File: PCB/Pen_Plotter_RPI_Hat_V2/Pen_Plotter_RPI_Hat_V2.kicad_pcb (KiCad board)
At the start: 4 copper layers, 85 x 56 mm, 28 parts, among them J1 RASM712PX, J2 X_LIMIT_SWITCH, J3 X-AXIS_STEPPER, J4 Y_LIMIT_SWITCH, J5 SERVO, J6 Y-AXIS_STEPPER, J7 PAPER_SENSOR, J8 DC_MOTOR, U2 MINI560, U4 X-AXIS_DRV8825_STEPPER_MOTOR_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, U5 Y-AXIS_DRV8825_STEPPER_MOTOR_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, U6 RPI3-MODBP-BULK, U7 LM393AN, U9 ATmega328P-P

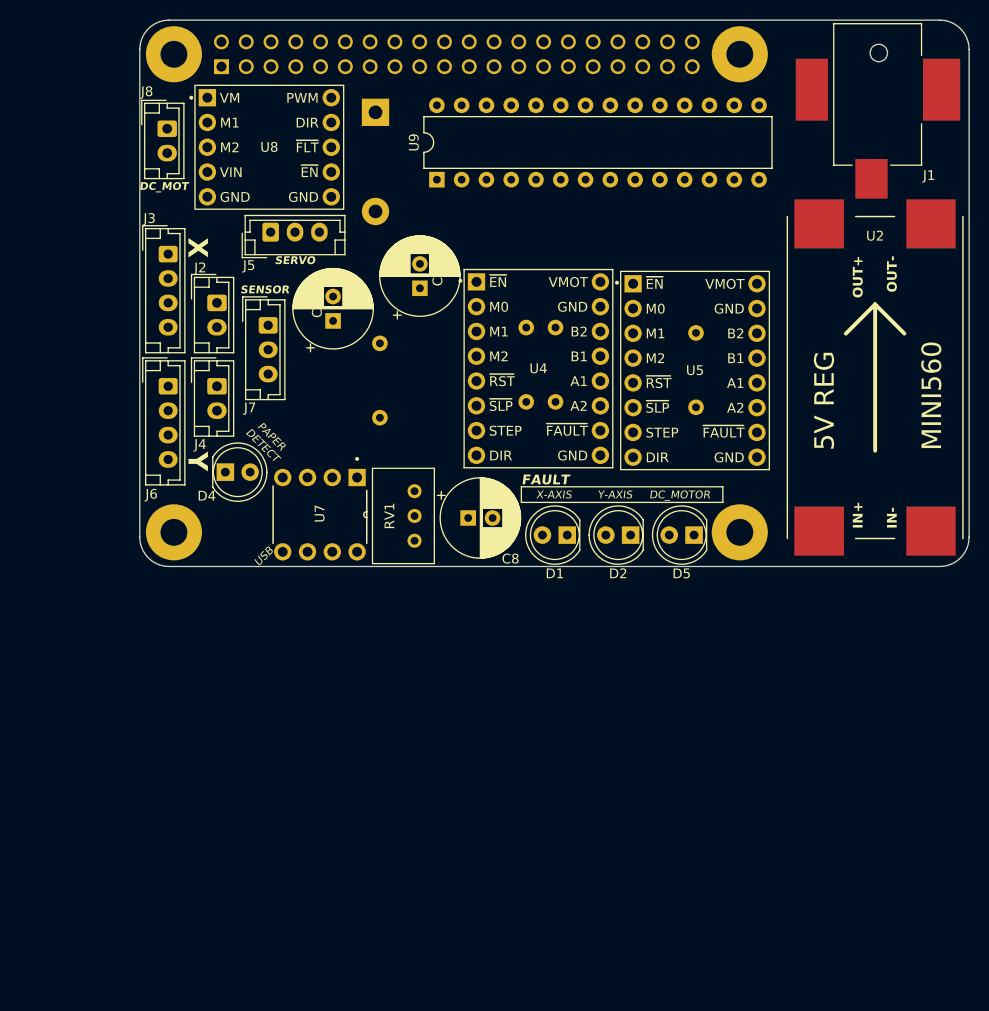
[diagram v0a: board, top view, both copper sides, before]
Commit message: Added third stepper motor driver
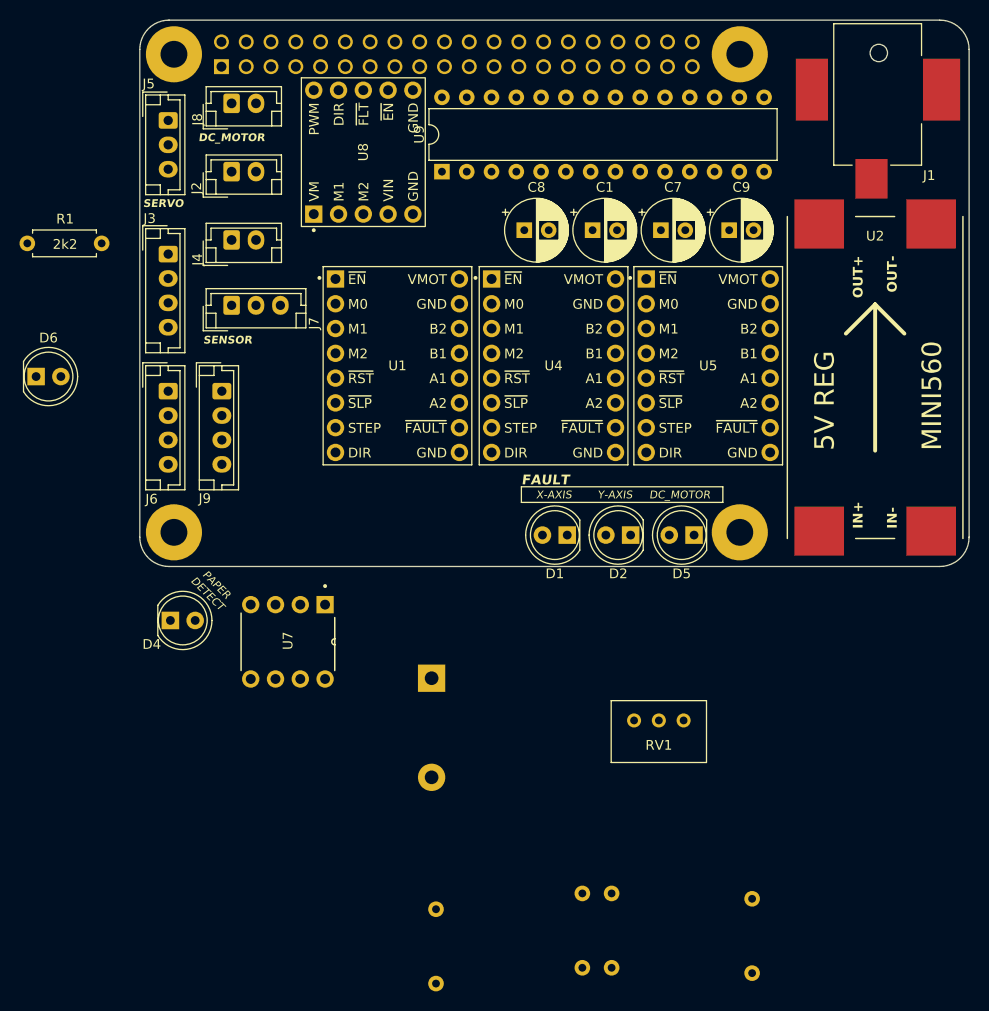
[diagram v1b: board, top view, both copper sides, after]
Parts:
- added C1: 100u, Capacitor_THT:CP_Radial_D6.3mm_P2.50mm, F.Cu at (102.5, 56.0)
- added D6: RED, LED_THT:LED_D5.0mm, F.Cu at (45.5, 71.0)
- added J9: EXTRA_STEPPER, Connector_JST:JST_EH_B4B-EH-A_1x04_P2.50mm_Vertical, F.Cu at (64.5, 72.5)
- added R1: 2k2, Pen_Plotter_Lib:THT_RESISTOR_WITH_VALUE, F.Cu at (48.4, 57.5)
- added U1: EXTRA_DRV8825_STEPPER_MOTOR_DRIVER_CARRIER, Pen_Plotter_Lib:IC_DRV8825_STEPPER_MOTOR_DRIVER_CARRIER, F.Cu at (82.5, 69.9)
- C7, C8, C9: footprint Capacitor_THT:CP_Radial_D8.0mm_P2.50mm -> Capacitor_THT:CP_Radial_D6.3mm_P2.50mm
- moved D3 58.3 mm to (86.0, 101.9)
- moved R3 58.3 mm to (101.5, 127.8)
- moved R4 58.3 mm to (104.5, 127.8)
- moved R5 58.3 mm to (86.5, 129.5)
- moved R6 58.3 mm to (119.0, 128.4)
- moved C7 34.9 mm to (109.5, 56.0), turned to 0 degrees
- moved RV1 33.2 mm to (111.8, 106.2), turned to 0 degrees
- moved C9 32.3 mm to (116.5, 56.0), turned to 0 degrees
- moved C8 30.1 mm to (95.5, 56.0)
- moved D4 16.2 mm to (59.2, 96.0)
- moved J5 15.5 mm to (59.0, 44.8), turned to -90 degrees
- moved J4 15.1 mm to (65.5, 57.0), turned to 0 degrees
- moved J2 13.5 mm to (65.5, 50.0), turned to 0 degrees
- moved U7 13.4 mm to (67.5, 102.0)
- moved U8 9.65 mm to (79.0, 48.0), turned to 90 degrees
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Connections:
- J3 pad 1: /Stepper Motors/X-AXIS_A1 -> /Stepper Motors/X-AXIS_A2
- J3 pad 2: /Stepper Motors/X-AXIS_A2 -> /Stepper Motors/X-AXIS_A1
- J6 pad 1: /Stepper Motors/Y-AXIS_A1 -> /Stepper Motors/Y-AXIS_A2
- J6 pad 2: /Stepper Motors/Y-AXIS_A2 -> /Stepper Motors/Y-AXIS_A1
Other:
- board text removed: "DC_MOT"
- board text removed: "USB"
- board text removed: "X"
- board text removed: "Y"

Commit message: Completed PCB layout
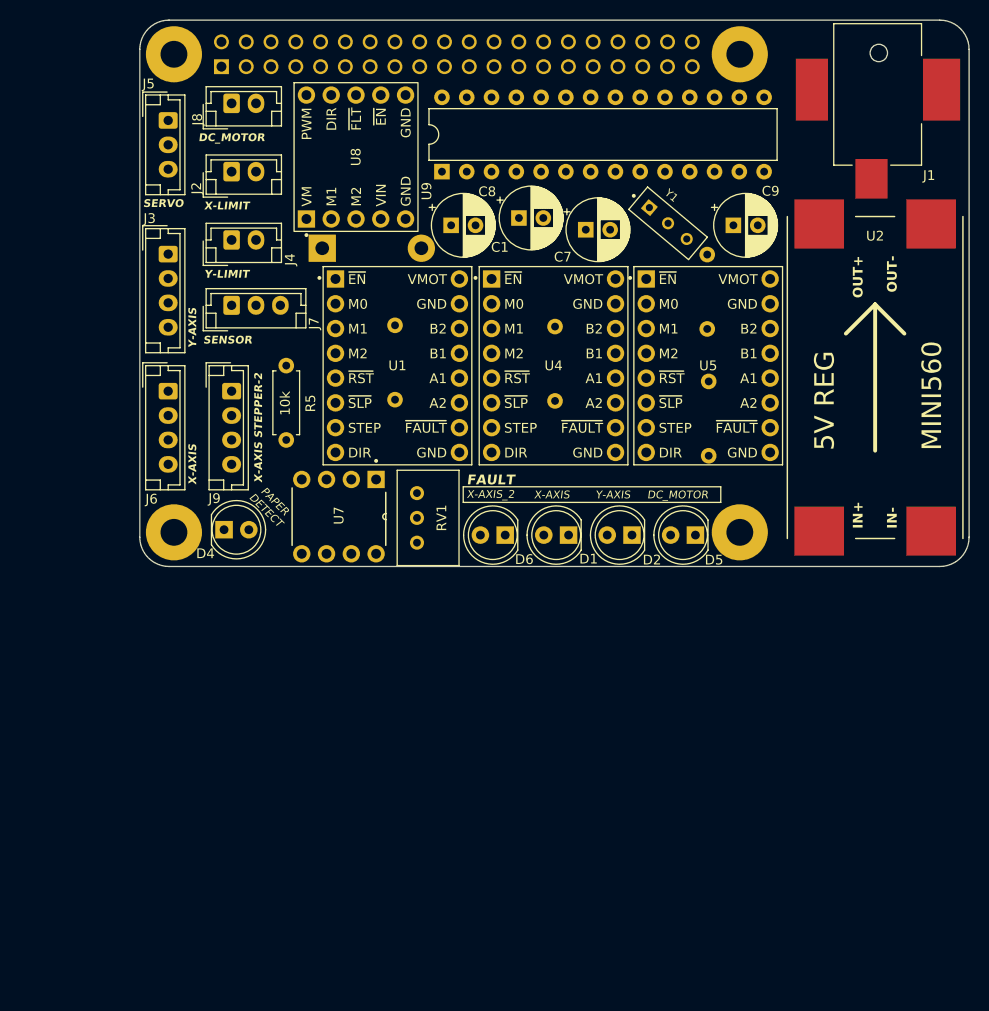
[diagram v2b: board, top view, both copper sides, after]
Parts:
- added Y1: CSTLS8M00G56-A0, Pen_Plotter_Lib:OSC_CSTLS8M00G56-A0, F.Cu at (110.2, 55.3)
- R1: moved to B.Cu
- R5: moved to F.Cu
- moved R6 66.2 mm to (114.3, 62.4)
- moved R3 58.2 mm to (98.8, 69.8)
- moved R5 57.8 mm to (71.0, 73.8)
- moved R4 53.4 mm to (114.5, 75.4)
- moved D6 50.8 mm to (93.5, 87.2), turned to 180 degrees
- moved D3 45.5 mm to (74.8, 57.9), turned to 0 degrees
- moved RV1 35.9 mm to (84.5, 83.0), turned to 90 degrees
- moved R1 35.8 mm to (82.2, 69.5), turned to 90 degrees
- moved U7 13.9 mm to (72.7, 89.2)
- moved D4 10.8 mm to (64.7, 86.7)
- moved C7 7.70 mm to (101.8, 56.0)
- moved C1 7.65 mm to (95.0, 54.8)
- moved C8 7.52 mm to (88.0, 55.5)
- moved J9 1.00 mm to (65.5, 72.5)
- moved U8 0.90 mm to (78.2, 48.5)
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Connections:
- U9 pad 10: unconnected-(U9-XTAL2/PB7-Pad10) -> Net-(U9-XTAL2/PB7)
- U9 pad 9: unconnected-(U9-XTAL1/PB6-Pad9) -> Net-(U9-XTAL1/PB6)
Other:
- board text added: "X-AXIS STEPPER-2"
- board text added: "X-AXIS_2"
- board text added: "X-LIMIT"
- board text added: "Y-LIMIT"

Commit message: Manually added traces for high current
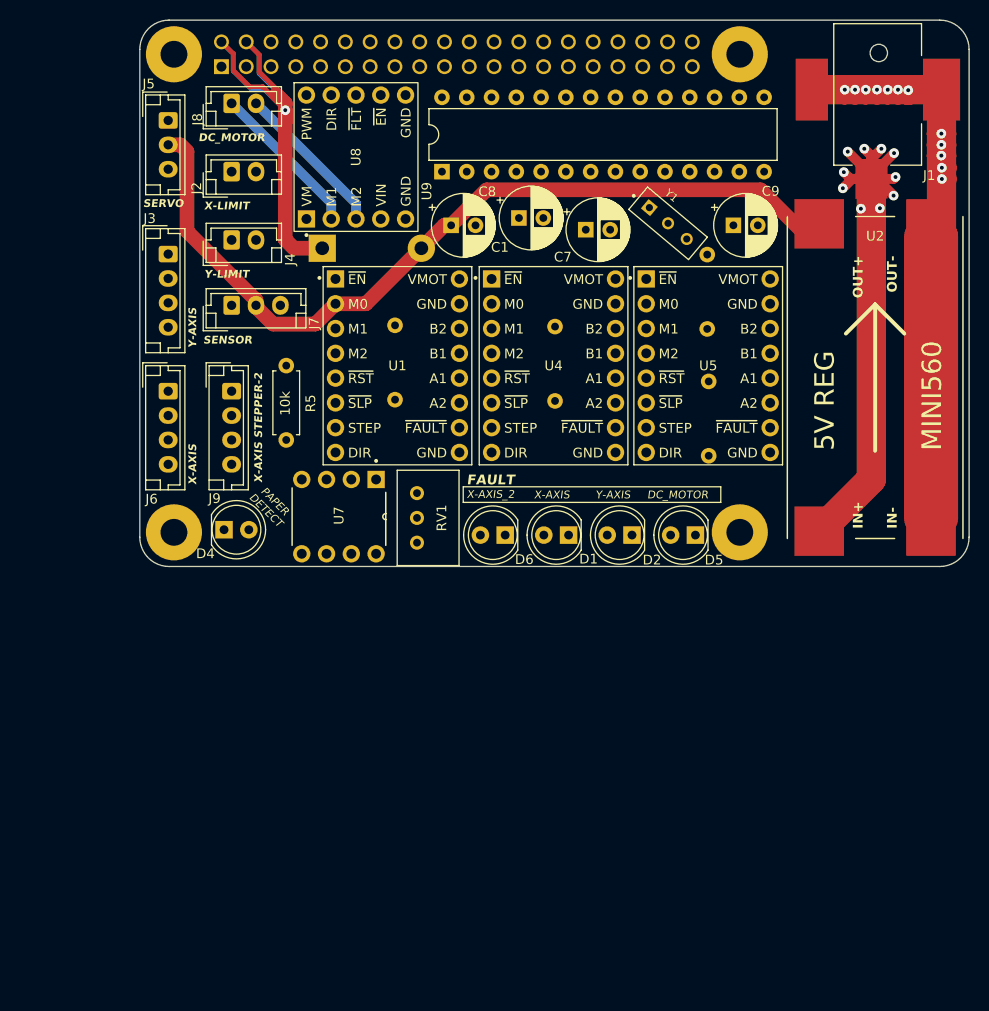
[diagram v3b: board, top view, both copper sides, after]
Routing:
- net GND: track 0.00 -> 86.5 mm, vias 0 -> 12
- net +5V: track 0.00 -> 85.9 mm
- net +12V: track 0.00 -> 69.7 mm, vias 0 -> 10
- net Net-(D3-K): track 0.00 -> 55.7 mm, vias 0 -> 1
- net Net-(J8-Pin_2): track 0.00 -> 16.1 mm
- net Net-(J8-Pin_1): track 0.00 -> 16.1 mm

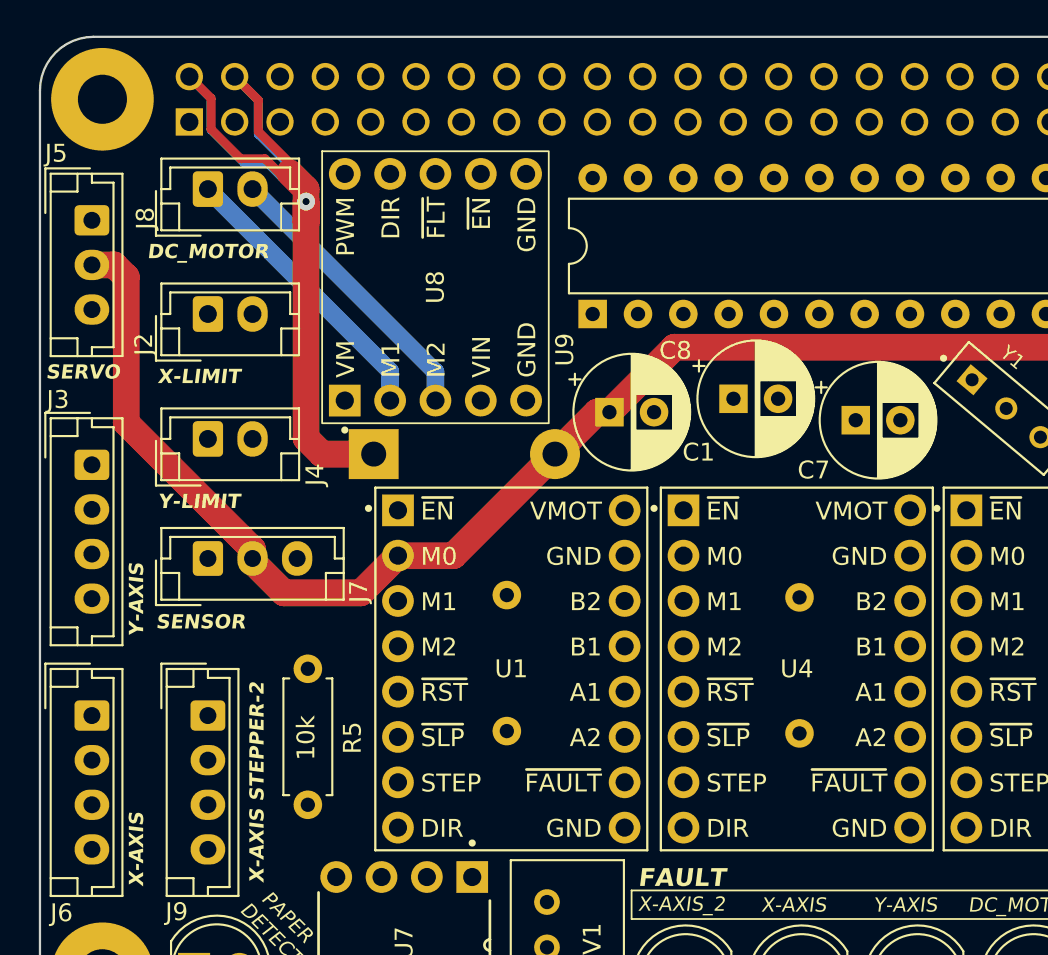
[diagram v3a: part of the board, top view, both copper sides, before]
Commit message: Changed layout and footprints to make routing easier
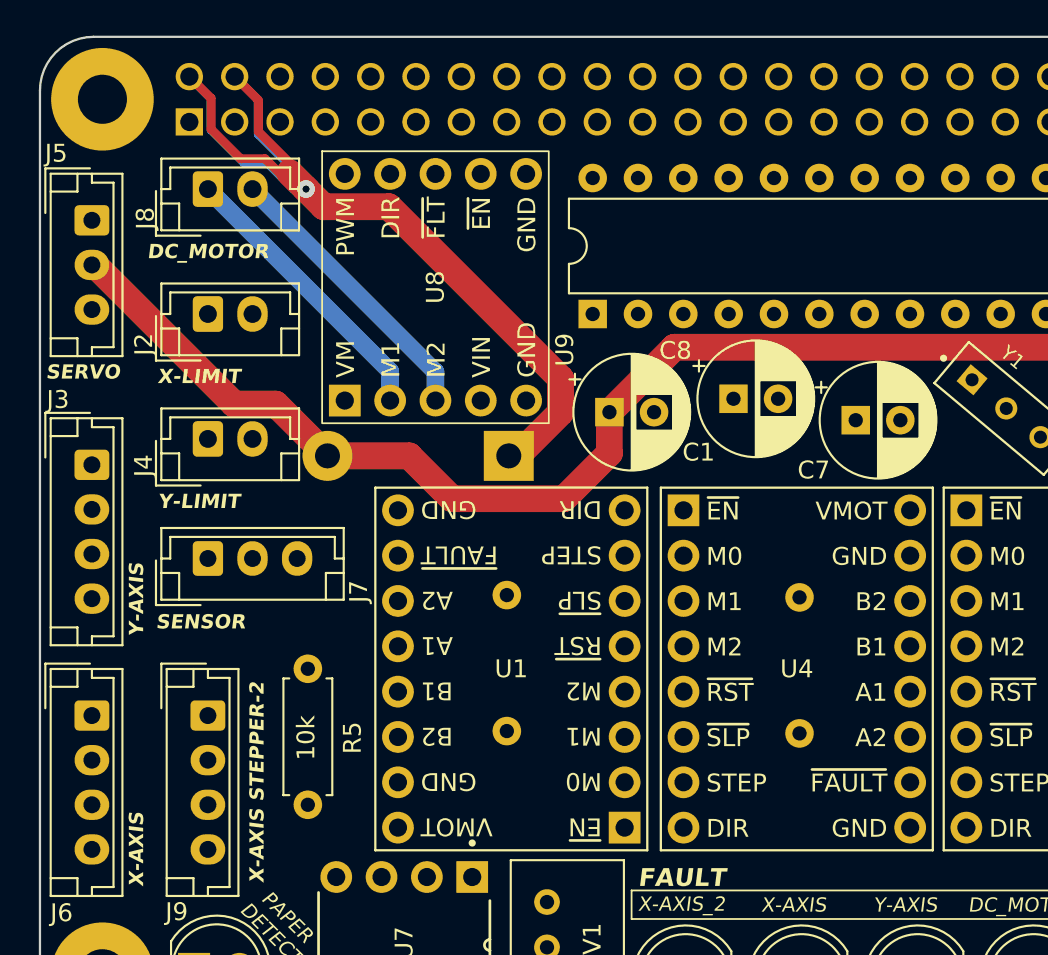
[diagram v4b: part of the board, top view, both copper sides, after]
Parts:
- moved D3 7.57 mm to (82.4, 58.0), turned to 180 degrees
- turned U1 to 180 degrees
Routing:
- net +5V: track 85.9 -> 77.7 mm
- net Net-(D3-K): track 55.7 -> 59.4 mm

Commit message: Completed routing of circuit board
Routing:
- net +5V: track 77.7 -> 188.9 mm
- net /Stepper Motors/Y-AXIS_A2: track 0.00 -> 109.7 mm, vias 0 -> 3
- net +3V3: track 0.00 -> 99.6 mm
- net /Stepper Motors/X_AXIS_B1: track 0.00 -> 84.1 mm, vias 0 -> 1
- net /Stepper Motors/X-AXIS_B2: track 0.00 -> 83.6 mm, vias 0 -> 2
- net /Stepper Motors/Y-AXIS_B2: track 0.00 -> 76.1 mm, vias 0 -> 1
- net SERVO_PWM: track 0.00 -> 74.8 mm
- net /Stepper Motors/Y-AXIS_A1: track 0.00 -> 72.6 mm, vias 0 -> 1
- net /Stepper Motors/Y_AXIS_B1: track 0.00 -> 70.7 mm
- net /Raspberry Pi/DC_MOT_FLT: track 0.00 -> 70.6 mm, vias 0 -> 1
- net /Stepper Motors/X-AXIS_A2: track 0.00 -> 66.4 mm, vias 0 -> 1
- net Y_LIMIT: track 0.00 -> 66.1 mm, vias 0 -> 1
- net PAPER_SENSOR_OUT_3V3: track 0.00 -> 62.9 mm
- net STEPPER_EN: track 0.00 -> 61.9 mm
- net X_LIMIT: track 0.00 -> 60.1 mm, vias 0 -> 4
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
